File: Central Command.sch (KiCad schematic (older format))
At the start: 3 parts

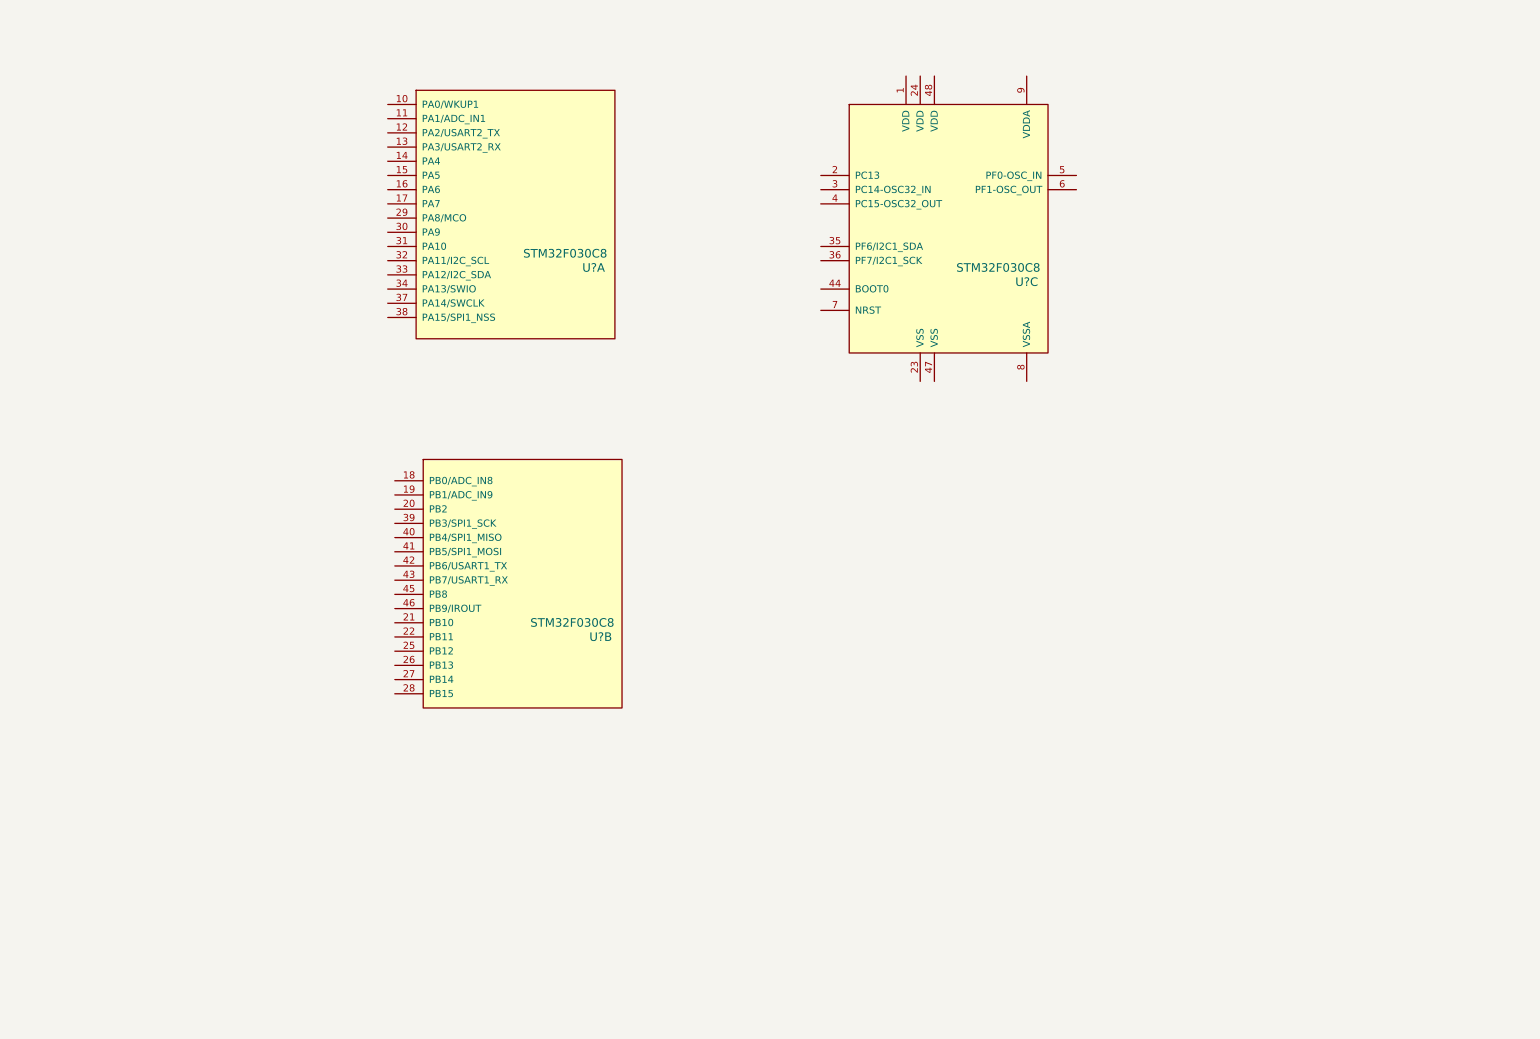
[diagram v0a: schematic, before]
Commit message: Added footprint for 3.3V fixed linear regulator and associated circuitry
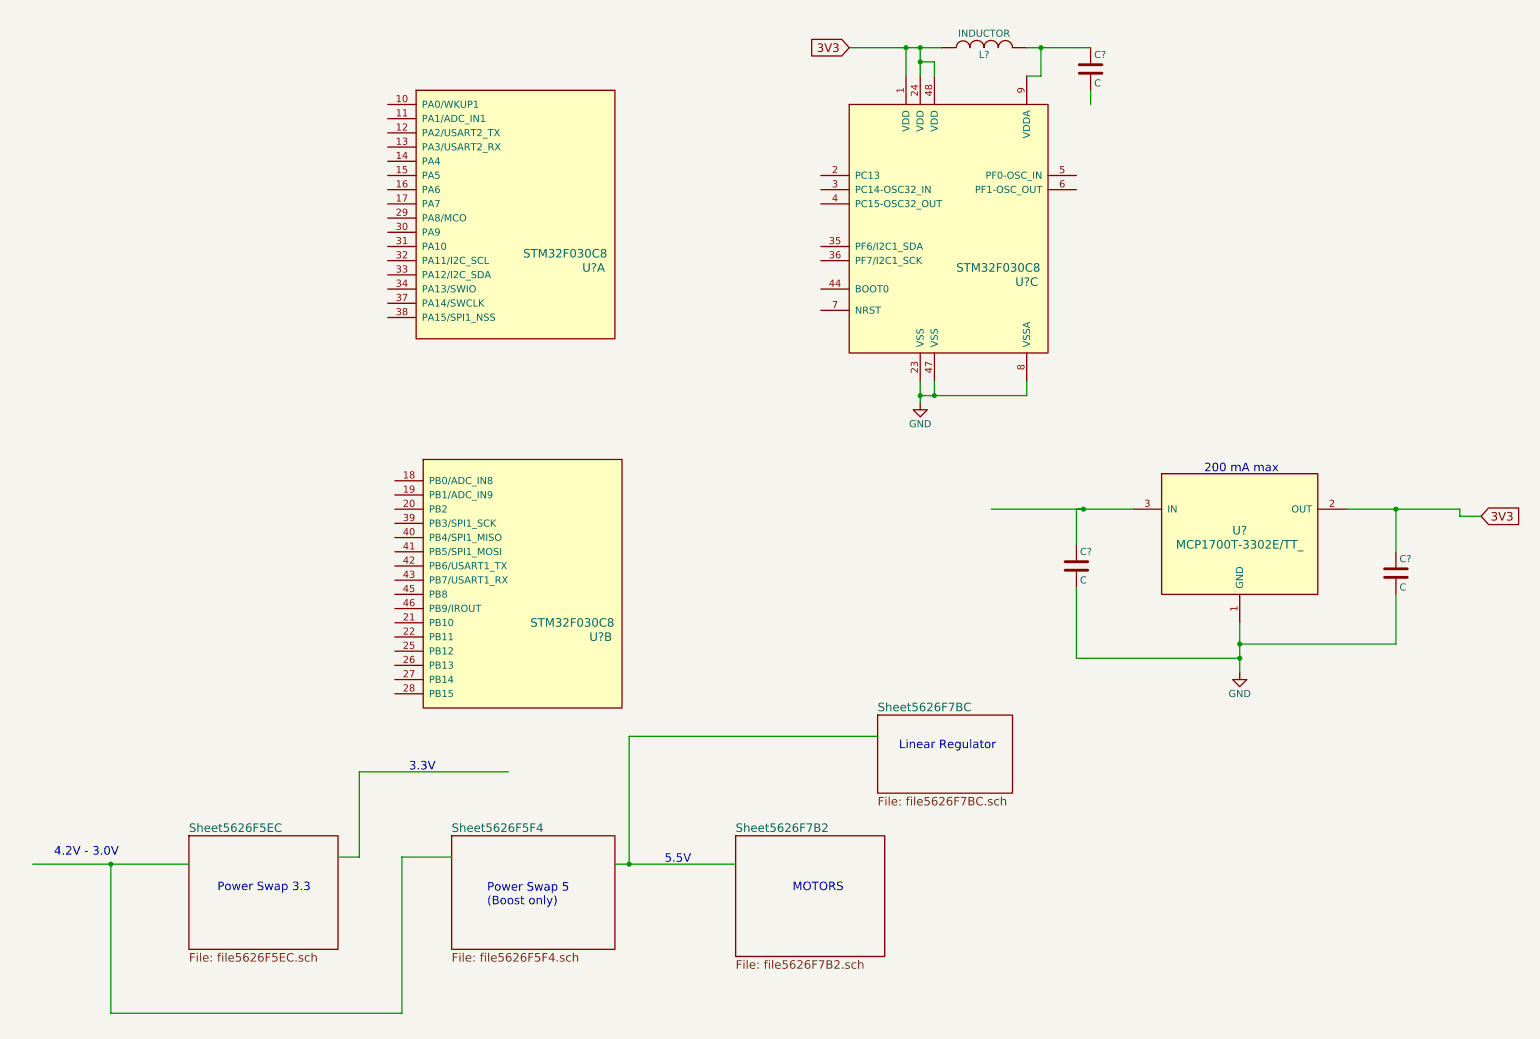
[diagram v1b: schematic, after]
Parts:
- added C? (x3): C, symbol C
- added L?: INDUCTOR, symbol INDUCTOR
- added U?: MCP1700T-3302E/TT_, symbol MCP1700T-3302E/TT_
- U? (x3): Link (none) -> http://parts.io/detail/153811934/STM32F030C8T6TR
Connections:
- net labels added: 3V3, GND
- wire segments 0 -> 36
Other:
- note added: "200 mA max"
- note added: "3.3V"
- note added: "4.2V - 3.0V"
- note added: "5.5V"
- note added: "Linear Regulator"
- note added: "MOTORS"
- note added: "Power Swap 3.3"
- note added: "Power Swap 5\n(Boost only)"
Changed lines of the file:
@@
 $Descr A4 11693 8268
 encoding utf-8
-Sheet 1 1
+Sheet 1 5
 Title ""
 Date ""
@@
 F 2 "" H 4000 1950 60  0000 C CNN
 F 3 "" H 4000 1950 60  0000 C CNN
+F 4 "http://parts.io/detail/153811934/STM32F030C8T6TR" H 4000 1950 60  0001 C CNN "Link"
 	1    4000 1950
 	1    0    0    -1
@@
 F 2 "" H 4050 4550 60  0000 C CNN
 F 3 "" H 4050 4550 60  0000 C CNN
+F 4 "http://parts.io/detail/153811934/STM32F030C8T6TR" H 4050 4550 60  0001 C CNN "Link"
 	2    4050 4550
 	1    0    0    -1
@@
 F 2 "" H 7050 2050 60  0000 C CNN
 F 3 "" H 7050 2050 60  0000 C CNN
+F 4 "http://parts.io/detail/153811934/STM32F030C8T6TR" H 7050 2050 60  0001 C CNN "Link"
 	3    7050 2050
 	1    0    0    -1
 $EndComp
+$Comp
+L INDUCTOR L?
+U 1 1 5626F24B
+P 7250 800
+F 0 "L?" V 7200 800 50  0000 C CNN
+F 1 "INDUCTOR" V 7350 800 50  0000 C CNN
+F 2 "" H 7250 800 60  0000 C CNN
+F 3 "" H 7250 800 60  0000 C CNN
+	1    7250 800
+	0    -1   -1   0
+$EndComp
+$Comp
+L C C?
+U 1 1 5626F380
+P 8000 950
+F 0 "C?" H 8025 1050 50  0000 L CNN
+F 1 "C" H 8025 850 50  0000 L CNN
+F 2 "" H 8038 800 30  0000 C CNN
+F 3 "" H 8000 950 60  0000 C CNN
+	1    8000 950
+	1    0    0    -1
+$EndComp
+Wire Wire Line
+	8000 800  7550 800
+Wire Wire Line
+	7550 1000 7650 1000
+Wire Wire Line
+	7650 1000 7650 800
+Connection ~ 7650 800
+Wire Wire Line
+	8000 1100 8000 1200
+Wire Wire Line
+	6300 800  6950 800
+Wire Wire Line
+	6700 800  6700 1000
+Wire Wire Line
+	6800 800  6800 1000
+Connection ~ 6800 800
+Wire Wire Line
+	6900 1000 6900 900
+Wire Wire Line
+	6900 900  6800 900
+Connection ~ 6800 900
+$Sheet
+S 1650 6350 1050 800
+U 5626F5ED
+F0 "Sheet5626F5EC" 60
+F1 "file5626F5EC.sch" 60
+$EndSheet
+$Sheet
+S 3500 6350 1150 800
+U 5626F5F5
+F0 "Sheet5626F5F4" 60
+F1 "file5626F5F4.sch" 60
+$EndSheet
+Wire Wire Line
+	550  6550 1650 6550
+Text Notes 700  6500 0    60   ~ 0
+4.2V - 3.0V
+Wire Wire Line
+	2700 6500 2850 6500
+Wire Wire Line
+	2850 6500 2850 5900
+Wire Wire Line
+	2850 5900 3900 5900
+Text Notes 3200 5900 0    60   ~ 0
+3.3V
+Wire Wire Line
+	1100 6550 1100 7600
+Wire Wire Line
+	1100 7600 3150 7600
+Wire Wire Line
+	3150 7600 3150 6500
+Wire Wire Line
+	3150 6500 3500 6500
+Connection ~ 1100 6550
+Wire Wire Line
+	4650 6550 5500 6550
+Text Notes 5000 6550 0    60   ~ 0
+5.5V
+$Sheet
+S 5500 6350 1050 850
+U 5626F7B3
+F0 "Sheet5626F7B2" 60
+F1 "file5626F7B2.sch" 60
+$EndSheet
+$Sheet
+S 6500 5500 950  550
+U 5626F7BD
+F0 "Sheet5626F7BC" 60
+F1 "file5626F7BC.sch" 60
+$EndSheet
+Text Notes 5900 6750 0    60   ~ 0
+MOTORS
+Text Notes 1850 6750 0    60   ~ 0
+Power Swap 3.3
+Text Notes 3750 6850 0    60   ~ 0
+Power Swap 5\n(Boost only)
+Wire Wire Line
+	4750 6550 4750 5650
+Wire Wire Line
+	4750 5650 6500 5650
+Connection ~ 4750 6550
+Text Notes 6650 5750 0    60   ~ 0
+Linear Regulator
+$Comp
+L MCP1700T-3302E/TT_ U?
+U 1 1 56270053
+P 9050 4200
+F 0 "U?" H 9050 4200 60  0000 C CNN
+F 1 "MCP1700T-3302E/TT_" H 9050 4100 60  0000 C CNN
+F 2 "" H 9050 4200 60  0000 C CNN
+F 3 "" H 9050 4200 60  0000 C CNN
+F 4 "http://parts.io/detail/1370896/MCP1700T-3302E%2FTT" H 9050 4200 60  0001 C CNN "Link"
+	1    9050 4200
+	1    0    0    -1
+$EndComp
+$Comp
+L C C?
+U 1 1 5627009A
+P 7900 4450
+F 0 "C?" H 7925 4550 50  0000 L CNN
+F 1 "C" H 7925 4350 50  0000 L CNN
+F 2 "" H 7938 4300 30  0000 C CNN
+F 3 "" H 7900 4450 60  0000 C CNN
+	1    7900 4450
+	1    0    0    -1
+$EndComp
+$Comp
+L C C?
+U 1 1 56270119
+P 10150 4500
+F 0 "C?" H 10175 4600 50  0000 L CNN
+F 1 "C" H 10175 4400 50  0000 L CNN
+F 2 "" H 10188 4350 30  0000 C CNN
+F 3 "" H 10150 4500 60  0000 C CNN
+	1    10150 4500
+	1    0    0    -1
+$EndComp
+$Comp
+L GND #PWR?
+U 1 1 562701EB
+P 9050 5200
+F 0 "#PWR?" H 9050 4950 50  0001 C CNN
+F 1 "GND" H 9050 5050 50  0000 C CNN
+F 2 "" H 9050 5200 60  0000 C CNN
+F 3 "" H 9050 5200 60  0000 C CNN
+	1    9050 5200
+	1    0    0    -1
+$EndComp
+Wire Wire Line
+	9050 5200 9050 4850
+Wire Wire Line
+	9050 5000 10150 5000
+Wire Wire Line
+	10150 5000 10150 4650
+Connection ~ 9050 5000
+Wire Wire Line
+	9050 5100 7900 5100
+Wire Wire Line
+	7900 5100 7900 4600
+Connection ~ 9050 5100
+Wire Wire Line
+	8300 4050 7300 4050
+Wire Wire Line
+	7900 4300 7900 4050
+Wire Wire Line
+	7900 4050 7950 4050
+Connection ~ 7950 4050
+Wire Wire Line
+	9800 4050 10600 4050
+Wire Wire Line
+	10150 4050 10150 4350
+Connection ~ 10150 4050
+Text GLabel 10750 4100 2    60   Input ~ 0
+3V3
+Wire Wire Line
+	10750 4100 10600 4100
+Wire Wire Line
+	10600 4100 10600 4050
+Text GLabel 6300 800  0    60   Input ~ 0
+3V3
+Connection ~ 6700 800
+$Comp
+L GND #PWR?
+U 1 1 5627066D
+P 6800 3300
+F 0 "#PWR?" H 6800 3050 50  0001 C CNN
+F 1 "GND" H 6800 3150 50  0000 C CNN
+F 2 "" H 6800 3300 60  0000 C CNN
+F 3 "" H 6800 3300 60  0000 C CNN
+	1    6800 3300
+	1    0    0    -1
+$EndComp
+Wire Wire Line
+	6800 3300 6800 3150
+Wire Wire Line
+	6800 3250 7550 3250
+Wire Wire Line
+	6900 3250 6900 3150
+Connection ~ 6800 3250
+Wire Wire Line
+	7550 3250 7550 3150
+Connection ~ 6900 3250
+Text Notes 8800 3800 0    60   ~ 0
+200 mA max
 $EndSCHEMATC

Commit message: Updated pinout names and added programming headers
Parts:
- added P?: CONN_01X06, symbol CONN_01X06
- added P?: CONN_01X02, symbol CONN_01X02
- added R? (x7): R, symbol R
- added R?: 0, symbol R
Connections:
- net labels added: NRST, TRACE
- wire segments 36 -> 57
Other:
- note added: "I2C1 DOES NOT EXIST FOR -C6 CHIP"
- note added: "PA2/PA3 will not have serial for the -C6 chip"
- note removed: "3.3V"
- note removed: "4.2V - 3.0V"
- note removed: "5.5V"
- note removed: "Linear Regulator"
- note removed: "MOTORS"
- note removed: "Power Swap 3.3"
- note removed: "Power Swap 5\n(Boost only)"

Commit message: Changed out schematic symbol to match schematic in CC11 video. Should have been saved last time.
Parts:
- removed U? (x3): STM32F030C8, symbol STM32F030C8
- added U? (x3): STM32F030C8, symbol STM32F030C8
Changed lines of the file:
@@
 EESchema Schematic File Version 2
+LIBS:Central Command-rescue
 LIBS:power
 LIBS:device
@@
 $EndDescr
 $Comp
-L STM32F030C8 U?
-U 1 1 561CB096
-P 4000 1950
-F 0 "U?" H 4500 1550 60  0000 C CNN
-F 1 "STM32F030C8" H 4300 1650 60  0000 C CNN
-F 2 "" H 4000 1950 60  0000 C CNN
-F 3 "" H 4000 1950 60  0000 C CNN
-F 4 "http://parts.io/detail/153811934/STM32F030C8T6TR" H 4000 1950 60  0001 C CNN "Link"
-	1    4000 1950
-	1    0    0    -1
-$EndComp
-$Comp
-L STM32F030C8 U?
-U 2 1 561CB127
-P 4050 4550
-F 0 "U?" H 4550 4150 60  0000 C CNN
-F 1 "STM32F030C8" H 4350 4250 60  0000 C CNN
-F 2 "" H 4050 4550 60  0000 C CNN
-F 3 "" H 4050 4550 60  0000 C CNN
-F 4 "http://parts.io/detail/153811934/STM32F030C8T6TR" H 4050 4550 60  0001 C CNN "Link"
-	2    4050 4550
-	1    0    0    -1
-$EndComp
-$Comp
-L STM32F030C8 U?
-U 3 1 561CB171
-P 7050 2050
-F 0 "U?" H 7550 1650 60  0000 C CNN
-F 1 "STM32F030C8" H 7350 1750 60  0000 C CNN
-F 2 "" H 7050 2050 60  0000 C CNN
-F 3 "" H 7050 2050 60  0000 C CNN
-F 4 "http://parts.io/detail/153811934/STM32F030C8T6TR" H 7050 2050 60  0001 C CNN "Link"
-	3    7050 2050
-	1    0    0    -1
-$EndComp
-$Comp
 L INDUCTOR L?
 U 1 1 5626F24B
@@
 Text Notes 2950 1000 0    60   ~ 12
 PA2/PA3 will not have serial for the -C6 chip
+$Comp
+L STM32F030C8 U?
+U 1 1 564E875E
+P 4000 1950
+F 0 "U?" H 4550 1000 60  0000 C CNN
+F 1 "STM32F030C8" H 4350 2850 60  0000 C CNN
+F 2 "" H 4000 1950 60  0000 C CNN
+F 3 "" H 4000 1950 60  0000 C CNN
+	1    4000 1950
+	1    0    0    -1
+$EndComp
+$Comp
+L STM32F030C8 U?
+U 2 1 564E8A03
+P 4100 4300
+F 0 "U?" H 4650 3350 60  0000 C CNN
+F 1 "STM32F030C8" H 4450 5200 60  0000 C CNN
+F 2 "" H 4100 4300 60  0000 C CNN
+F 3 "" H 4100 4300 60  0000 C CNN
+	2    4100 4300
+	1    0    0    -1
+$EndComp
+$Comp
+L STM32F030C8 U?
+U 3 1 564E8FF6
+P 7050 2050
+F 0 "U?" H 7600 1100 60  0000 C CNN
+F 1 "STM32F030C8" H 7400 2950 60  0000 C CNN
+F 2 "" H 7050 2050 60  0000 C CNN
+F 3 "" H 7050 2050 60  0000 C CNN
+	3    7050 2050
+	1    0    0    -1
+$EndComp
 $EndSCHEMATC
